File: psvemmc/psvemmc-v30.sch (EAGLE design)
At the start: 52 parts, among them J1 CON_HEADER_2X10-SHROUDED, J2 MF-CON-MICROUSB-RIGHT, U1 USB2244QFN, U2 LP3996_DSC_10, U3 TXS02612, U4 24AA00OT, U5 SN74AUP1G240DRY, U6 SN74AUP1G126DRY, U7 TPD4S014_DSQ_10, Y1 XRCGB

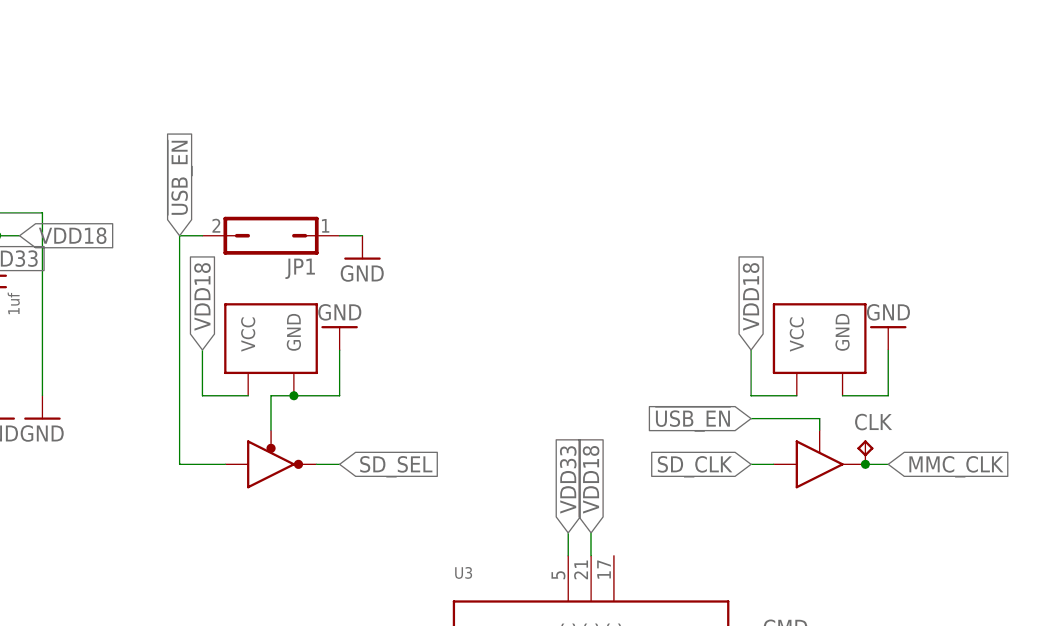
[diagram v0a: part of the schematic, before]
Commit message: psvemmc v3.1: fixed wrong pin ordering on clk buffer added pin 1 indicator to components missing them added title/value for sch in buffer components
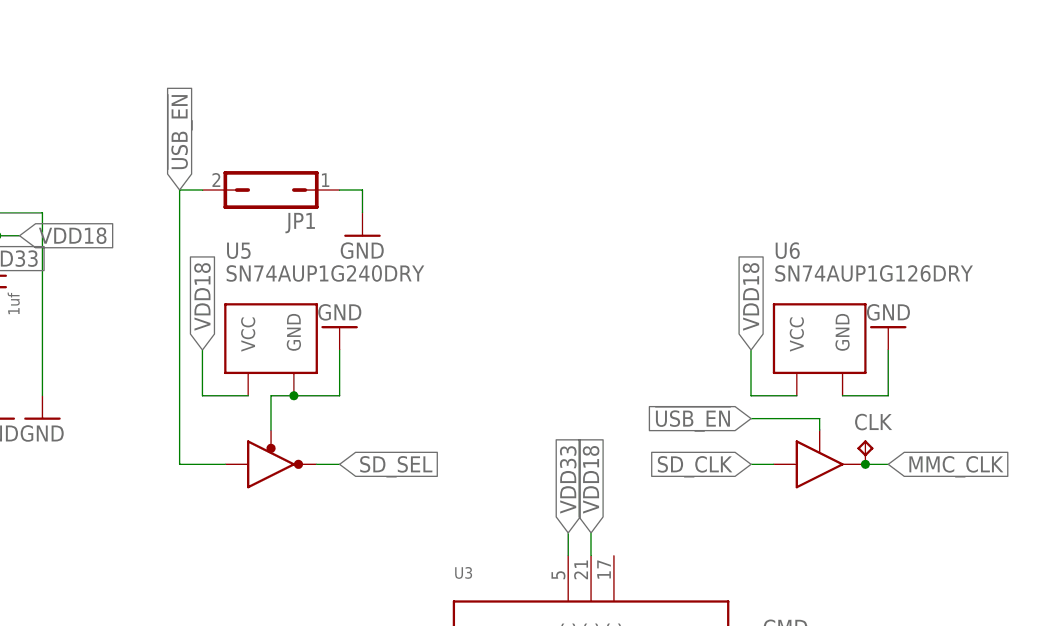
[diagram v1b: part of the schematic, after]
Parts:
- U5: device SN74LVC1G125:SN74AUP1G240DRY -> TI_Low_Power_Buffers:SN74AUP1G240DRY
- U6: device SN74LVC1G125:SN74AUP1G126DRY -> TI_Low_Power_Buffers:SN74AUP1G126DRY
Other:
- moved on the sheet: JP1
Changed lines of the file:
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@@
 <drawing>
 <settings>
-<setting alwaysvectorfont="yes"/>
+<setting alwaysvectorfont="no"/>
 <setting verticaltext="up"/>
 </settings>
@@
 <part name="FRAME1" library="frames" library_urn="urn:adsk.eagle:library:229" deviceset="A4L-LOC" device=""/>
 <part name="U1" library="USB2244" deviceset="USB2244" device="QFN"/>
-<part name="Y1" library="crystal" deviceset="XRCGB" device=""/>
+<part name="Y1" library="crystal" library_urn="urn:adsk.eagle:library:204" deviceset="XRCGB" device=""/>
 <part name="R1" library="Seeed-Resistor" deviceset="SMD-RES-1M-1%-1/10W(0603)" device="" value="1M"/>
 <part name="R2" library="Seeed-Resistor" deviceset="SMD-RES-12K-1%-1/10W(0603)" device="" value="12K"/>
@@
 <part name="GND24" library="supply1" library_urn="urn:adsk.eagle:library:371" deviceset="GND" device=""/>
 <part name="J2" library="MF_Connectors" deviceset="USB" device="_MICRO_RIGHT" value="MF-CON-MICROUSB-RIGHT"/>
-<part name="U5" library="SN74LVC1G125" deviceset="SN74AUP1G240" device="DRY" value="SN74AUP1G240DRY"/>
+<part name="U5" library="TI_Low_Power_Buffers" deviceset="SN74AUP1G240" device="DRY" value="SN74AUP1G240DRY"/>
 <part name="GND25" library="supply1" library_urn="urn:adsk.eagle:library:371" deviceset="GND" device=""/>
-<part name="U6" library="SN74LVC1G125" deviceset="SN74AUP1G126" device="DRY" value="SN74AUP1G126DRY"/>
+<part name="U6" library="TI_Low_Power_Buffers" deviceset="SN74AUP1G126" device="DRY" value="SN74AUP1G126DRY"/>
 <part name="GND13" library="supply1" library_urn="urn:adsk.eagle:library:371" deviceset="GND" device=""/>
 <part name="CLK" library="testpad" library_urn="urn:adsk.eagle:library:385" deviceset="TP" device="TP10R" package3d_urn="urn:adsk.eagle:package:27959/1"/>
@@
 <instance part="DAT2" gate="G$1" x="220.98" y="81.28"/>
 <instance part="DAT3" gate="G$1" x="220.98" y="78.74"/>
-<instance part="JP1" gate="A" x="165.1" y="137.16" rot="R90"/>
-<instance part="GND23" gate="1" x="175.26" y="134.62"/>
+<instance part="JP1" gate="A" x="165.1" y="142.24" rot="R90"/>
+<instance part="GND23" gate="1" x="175.26" y="137.16"/>
 <instance part="GND" gate="G$1" x="147.32" y="50.8"/>
 <instance part="U4" gate="G$1" x="142.24" y="66.04"/>
@@
 <segment>
 <pinref part="JP1" gate="A" pin="1"/>
-<wire x1="172.72" y1="137.16" x2="175.26" y2="137.16" width="0.1524" layer="91"/>
 <pinref part="GND23" gate="1" pin="GND"/>
+<wire x1="172.72" y1="142.24" x2="175.26" y2="142.24" width="0.1524" layer="91"/>
+<wire x1="175.26" y1="142.24" x2="175.26" y2="139.7" width="0.1524" layer="91"/>
 </segment>
 <segment>
@@
 <segment>
 <pinref part="JP1" gate="A" pin="2"/>
-<wire x1="157.48" y1="137.16" x2="154.94" y2="137.16" width="0.1524" layer="91"/>
-<label x="154.94" y="137.16" size="1.778" layer="95" rot="R90" xref="yes"/>
-<wire x1="154.94" y1="137.16" x2="154.94" y2="111.76" width="0.1524" layer="91"/>
+<label x="154.94" y="142.24" size="1.778" layer="95" rot="R90" xref="yes"/>
+<wire x1="154.94" y1="142.24" x2="154.94" y2="111.76" width="0.1524" layer="91"/>
 <pinref part="U5" gate="B" pin="A"/>
 <wire x1="154.94" y1="111.76" x2="160.02" y2="111.76" width="0.1524" layer="91"/>
-</segment>
-<segment>
+<wire x1="157.48" y1="142.24" x2="154.94" y2="142.24" width="0.1524" layer="91"/>
+</segment>
+<segment>
